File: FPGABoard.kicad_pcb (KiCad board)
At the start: 2 copper layers, 100 x 80 mm, 103 parts, among them P1 JTAG_FPGA, P2 UART, P3 USB_B, P4 CONN_02X07, P5 JTAG, P6 CONN_02X07, P7 CONN_02X07, P8 CONN_02X07, Q1 BSS123, SW1 SW_PUSH, SW2 SW_PUSH, SW3 SW_Push, SW4 SW_DIP_x02, U1 XC3S50A/VQ100, U2 LM317_SOT223, U3 LM317_SOT223, U4 LM317_SOT223, U5 ATMEGA32U4RC-A, U6 M25P20, U7 50MHz, Y1 16MHz

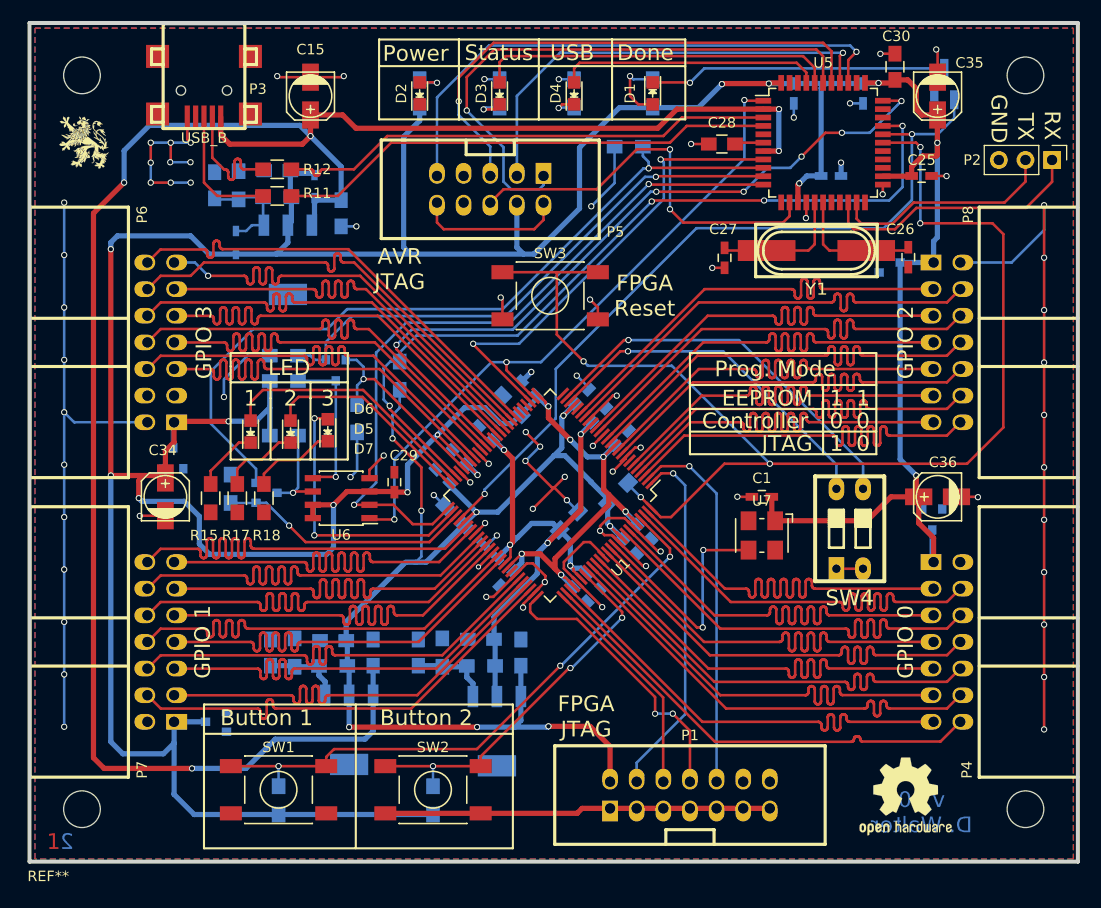
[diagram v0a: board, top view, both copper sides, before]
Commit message: Added Resistor in Reset Line
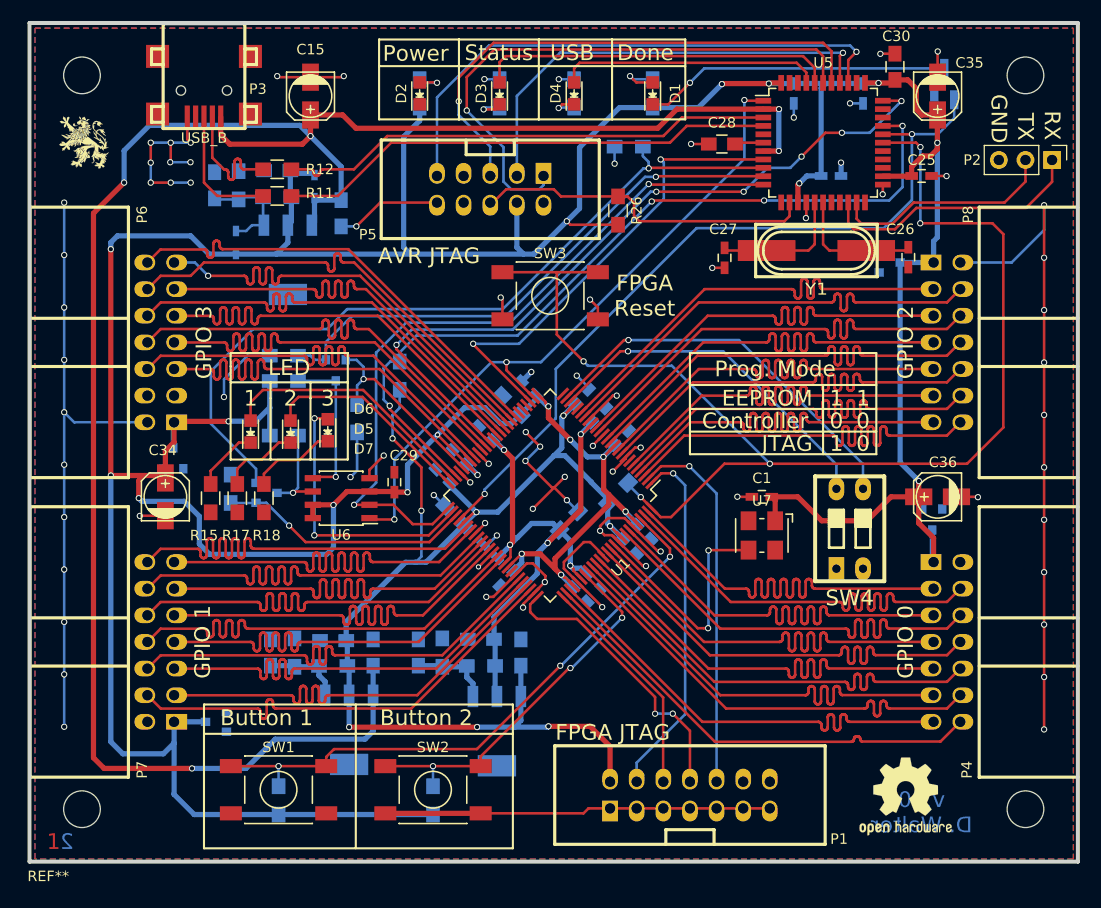
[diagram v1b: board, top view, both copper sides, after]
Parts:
- added R26: 10k, Resistors_SMD:R_0805_HandSoldering, F.Cu at (144.3, 78.2)
- U7: value 50MHz -> XO53
- turned D1 to 90 degrees
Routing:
- net GND: track 320.7 -> 308.0 mm
- net VCC: track 443.5 -> 449.5 mm, vias 20 -> 21
- net /Microcontroller/RESET: track 38.5 -> 32.6 mm, vias 2 -> 0
- net Net-(D1-Pad2): track 6.68 -> 4.69 mm
- net Net-(D1-Pad1): track 28.4 -> 29.3 mm

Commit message: Release for Manufacture
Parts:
- SW1, SW2, SW3: footprint SMD_Switch_LSX1301:SW_LSx_1301 -> Buttons_Switches_SMD:SW_SPST_B3S-1000
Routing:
- net GND: track 308.0 -> 322.7 mm
- net /Microcontroller/PROG_B: track 119.1 -> 121.0 mm
- net /Connections/BTN2: track 36.5 -> 35.6 mm
- net /Connections/BTN1: track 57.3 -> 56.8 mm

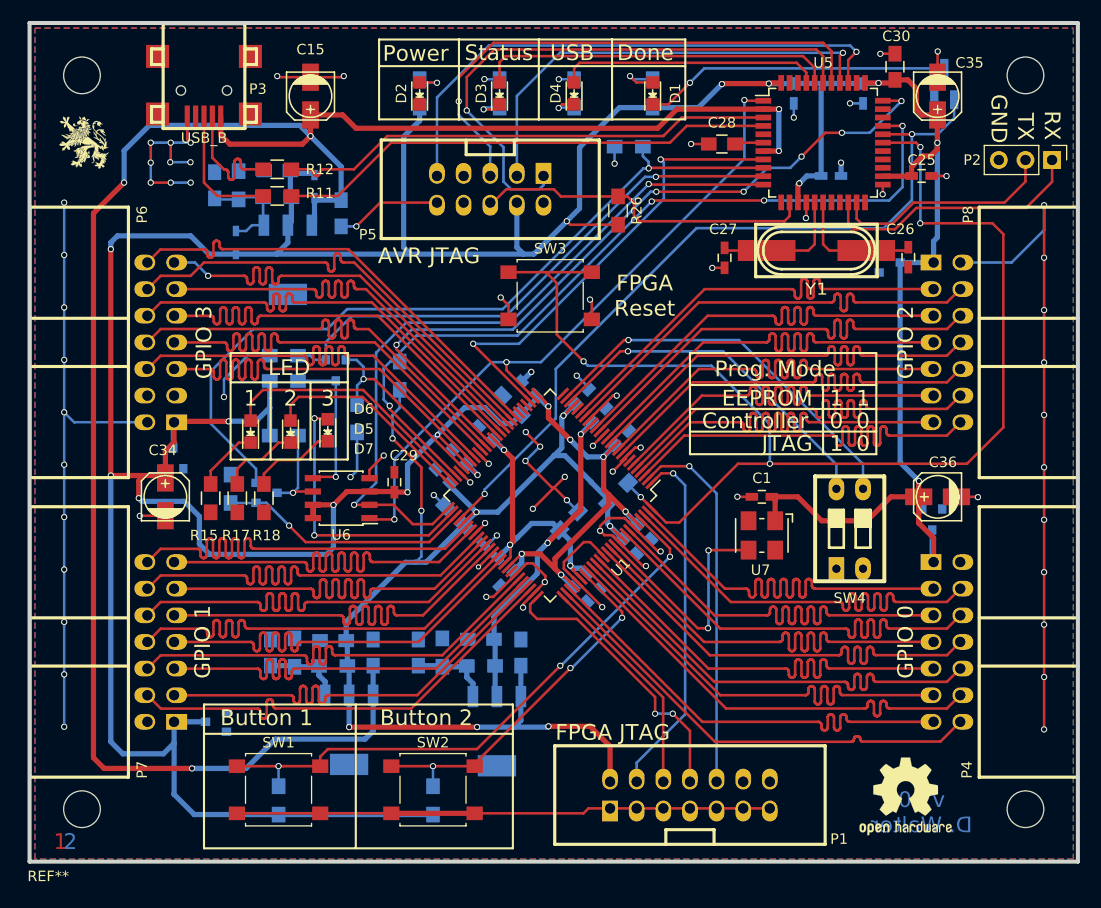
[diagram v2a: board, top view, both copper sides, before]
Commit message: Updated KiCad
After update to Kicad 5
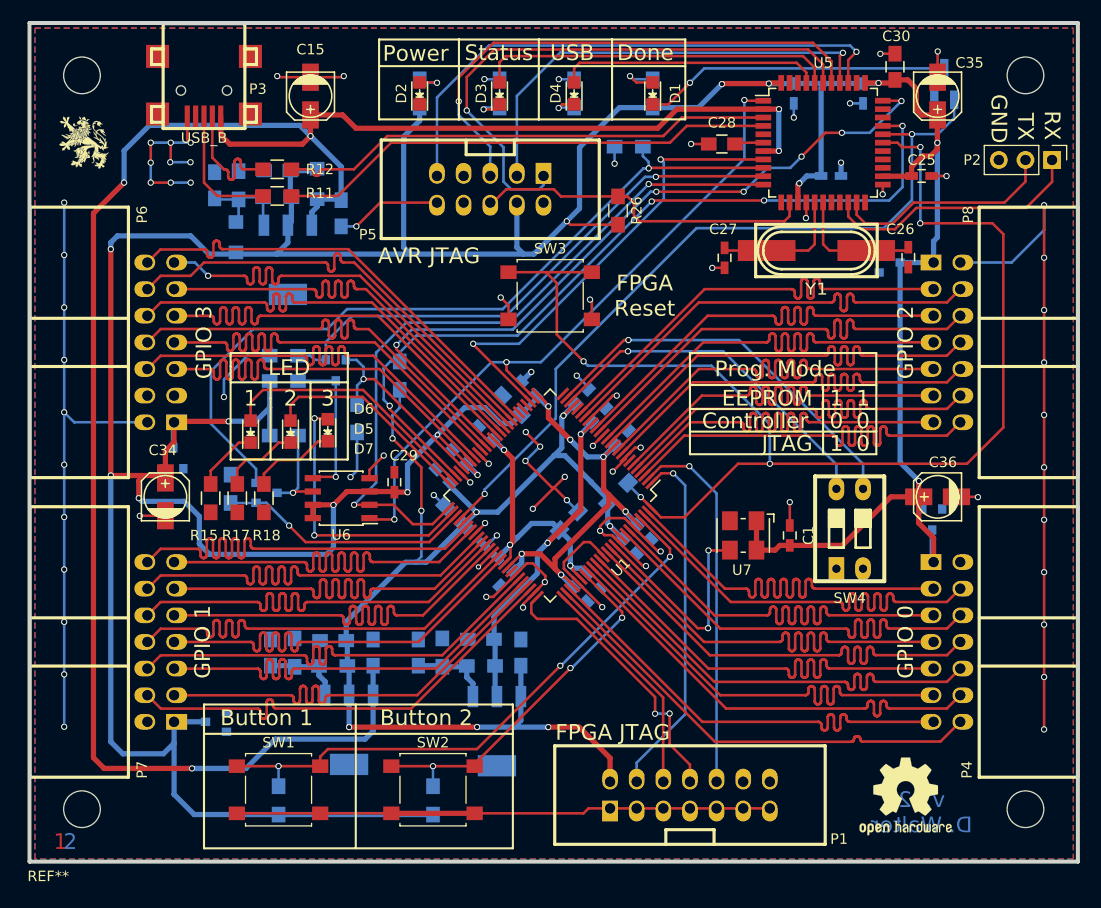
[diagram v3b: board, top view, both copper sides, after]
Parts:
- D8, D9: footprint w_smd_diode:sod323 -> w_smd_diode:do219ab
- moved C1 4.55 mm to (160.7, 109.2), turned to 90 degrees
- moved U7 1.78 mm to (156.2, 109.2)
- moved D9 0.51 mm to (107.8, 80.8)
- moved D8 0.36 mm to (115.6, 75.7)
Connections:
- U7 pad 4: (no net) -> VCC
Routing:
- net VCC: track 449.5 -> 451.7 mm
- net Net-(U1-Pad90): track 23.5 -> 21.7 mm
- net GND: track 322.7 -> 323.5 mm
- net Net-(C37-Pad1): track 10.4 -> 9.70 mm
- net VCC_AUX: track 115.5 -> 114.8 mm
- net /Microcontroller/TMS: track 50.9 -> 50.4 mm
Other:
- board text added: "v1.2 D. Walter"
- board text removed: "v1.0 D. Walter"
